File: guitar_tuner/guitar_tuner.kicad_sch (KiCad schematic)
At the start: 0 parts

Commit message: ESP32
ESP32 Addition
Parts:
- added C3, C4, C6: .1uF, symbol Device:C
- added C5: 1uF, symbol Device:C
- added R1: 10k, symbol Device:R
- added SW1: Reset, symbol Switch:SW_Omron_B3FS
- added SW2: Boot, symbol Switch:SW_Omron_B3FS
- added U1: ESP32-S2-SOLO, PCM_Espressif:ESP32-S2-SOLO, symbol esp32:ESP32-S2-SOLO
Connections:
- new net: C4.1, SW2.1, U1.39 (GPIO1/TOUCH1/ADC1_CH0)
- new net +3.3V: C3.2, C5.2, C6.2, R1.1, R1.2, SW1.2, U1.2 (3V3), U1.3 (EN)
- new net GND: C3.1, C4.2, C5.1, C6.1, SW1.1, SW2.2, U1.1 (GND), U1.40 (GND), U1.41 (GND)
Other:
- note added: "ESP32S2"

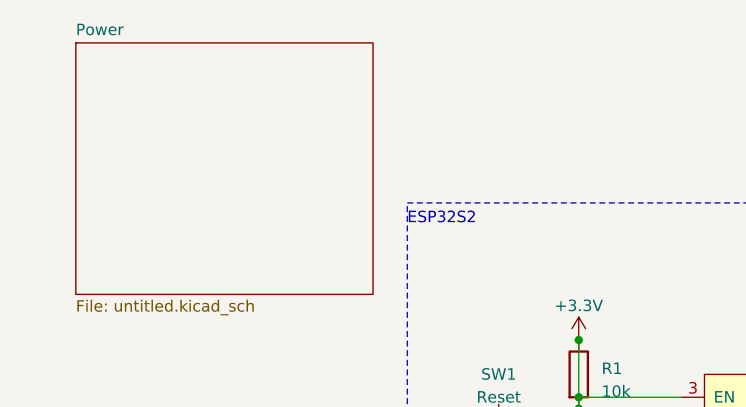
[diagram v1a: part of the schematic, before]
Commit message: Added micro USB B for input power as well as voltage regulator.
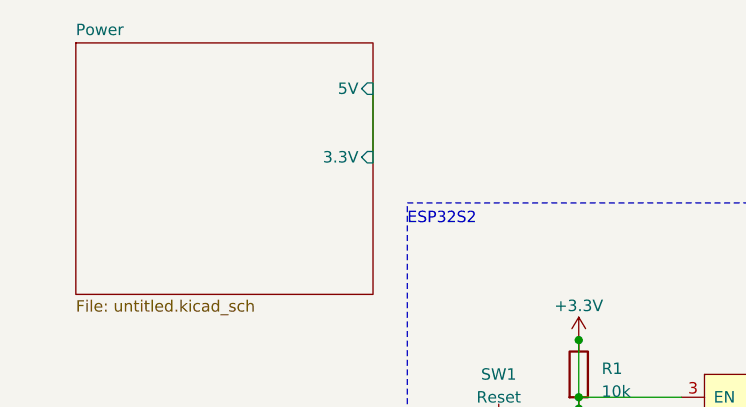
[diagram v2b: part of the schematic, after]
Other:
- sheet Power ports: added 3.3V, 5V; removed none
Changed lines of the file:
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@@
+	(wire
+		(pts
+			(xy 57.15 27.94) (xy 57.15 35.56)
+		)
+		(stroke
+			(width 0)
+			(type default)
+		)
+	)
 	(wire
 		(pts
@@
 			)
 		)
+		(pin "5V" input
+			(at 57.15 27.94 0)
+			(effects
+				(font
+					(size 1.27 1.27)
+				)
+				(justify right)
+			)
+		)
+		(pin "3.3V" input
+			(at 57.15 35.56 0)
+			(effects
+				(font
+					(size 1.27 1.27)
+				)
+				(justify right)
+			)
+		)

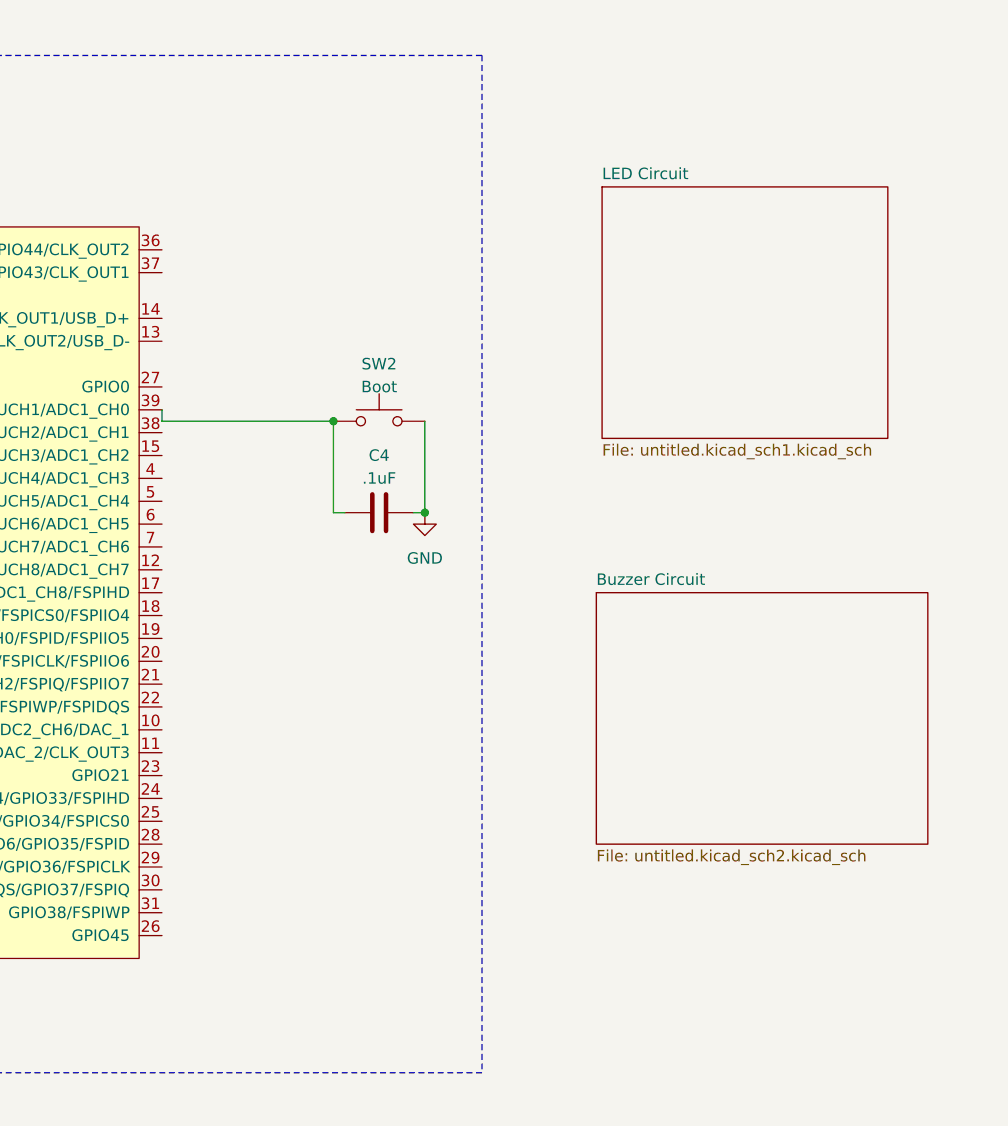
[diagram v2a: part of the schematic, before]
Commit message: LED
Addition of LED Circuits
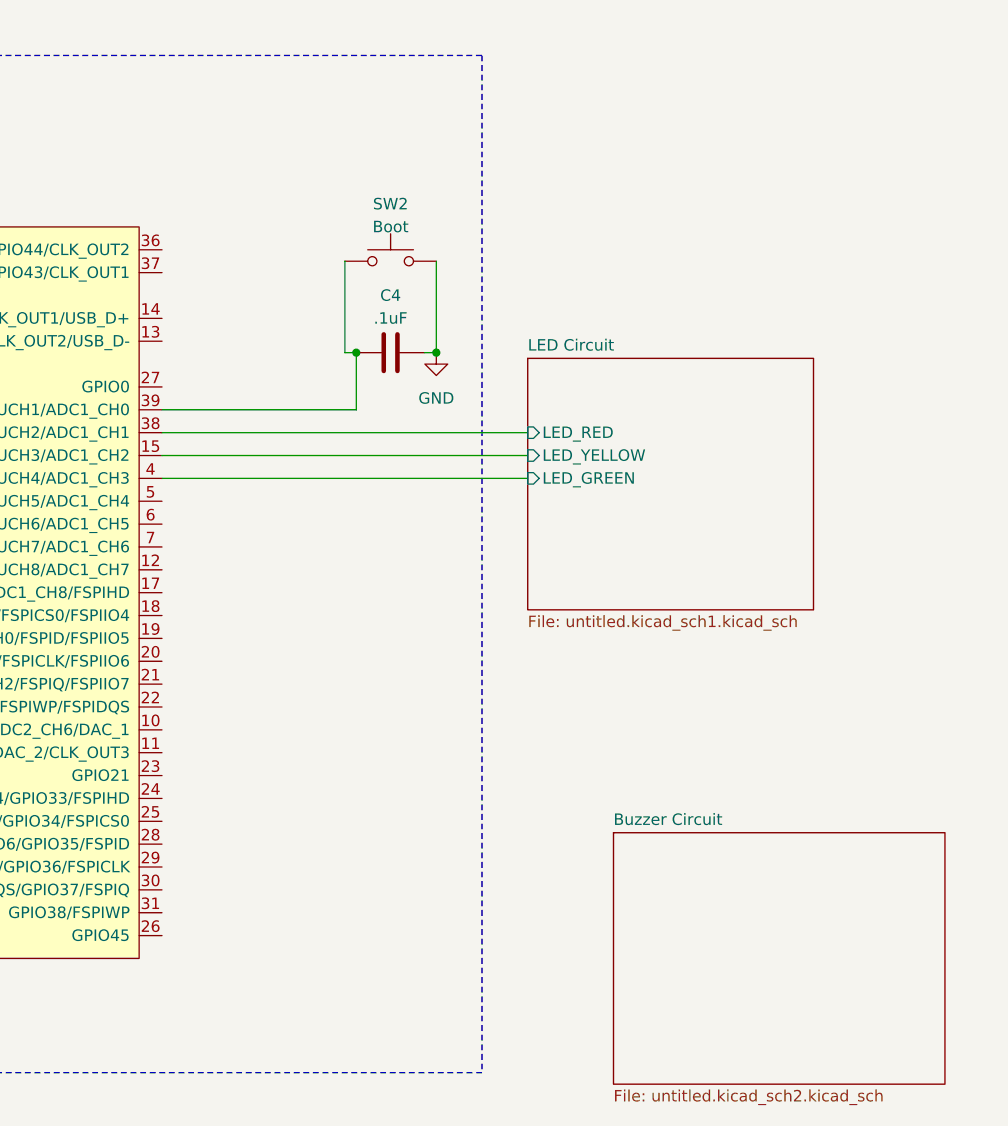
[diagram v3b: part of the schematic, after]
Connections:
- net LED Circuit/LED_YELLOW: now reaches U1.15 (GPIO3/TOUCH3/ADC1_CH2)
- net LED Circuit/LED_RED: now reaches U1.38 (GPIO2/TOUCH2/ADC1_CH1)
- net LED Circuit/LED_GREEN: now reaches U1.4 (GPIO4/TOUCH4/ADC1_CH3)
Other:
- sheet LED Circuit ports: added LED_GREEN, LED_RED, LED_YELLOW; removed none
- moved on the sheet: C4, SW2
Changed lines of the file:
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@@
 	)
 	(junction
-		(at 212.09 91.44)
-		(diameter 0)
-		(color 0 0 0 0)
-	)
-	(junction
-		(at 201.93 81.28)
+		(at 213.36 73.66)
 		(diameter 0)
 		(color 0 0 0 0)
@@
 		(color 0 0 0 0)
 	)
+	(junction
+		(at 204.47 73.66)
+		(diameter 0)
+		(color 0 0 0 0)
+	)
 	(wire
 		(pts
@@
 	(wire
 		(pts
-			(xy 203.2 91.44) (xy 201.93 91.44)
-		)
-		(stroke
-			(width 0)
-			(type default)
-		)
-	)
-	(wire
-		(pts
-			(xy 212.09 91.44) (xy 210.82 91.44)
+			(xy 204.47 73.66) (xy 203.2 73.66)
+		)
+		(stroke
+			(width 0)
+			(type default)
+		)
+	)
+	(wire
+		(pts
+			(xy 182.88 87.63) (xy 223.52 87.63)
+		)
+		(stroke
+			(width 0)
+			(type default)
+		)
+	)
+	(wire
+		(pts
+			(xy 213.36 73.66) (xy 212.09 73.66)
 		)
 		(stroke
@@
 	(wire
 		(pts
+			(xy 204.47 73.66) (xy 204.47 80.01)
+		)
+		(stroke
+			(width 0)
+			(type default)
+		)
+	)
+	(wire
+		(pts
+			(xy 182.88 80.01) (xy 204.47 80.01)
+		)
+		(stroke
+			(width 0)
+			(type default)
+		)
+	)
+	(wire
+		(pts
 			(xy 80.01 62.23) (xy 91.44 62.23)
 		)
@@
 	(wire
 		(pts
-			(xy 212.09 81.28) (xy 212.09 91.44)
-		)
-		(stroke
-			(width 0)
-			(type default)
-		)
-	)
-	(wire
-		(pts
-			(xy 182.88 81.28) (xy 201.93 81.28)
+			(xy 213.36 63.5) (xy 213.36 73.66)
 		)
 		(stroke
@@
 	(wire
 		(pts
-			(xy 201.93 81.28) (xy 201.93 91.44)
+			(xy 203.2 63.5) (xy 203.2 73.66)
+		)
+		(stroke
+			(width 0)
+			(type default)
+		)
+	)
+	(wire
+		(pts
+			(xy 182.88 82.55) (xy 223.52 82.55)
+		)
+		(stroke
+			(width 0)
+			(type default)
+		)
+	)
+	(wire
+		(pts
+			(xy 182.88 85.09) (xy 223.52 85.09)
 		)
 		(stroke
@@
 		(pts
 			(xy 80.01 66.04) (xy 76.2 66.04)
-		)
-		(stroke
-			(width 0)
-			(type default)
-		)
-	)
-	(wire
-		(pts
-			(xy 182.88 80.01) (xy 182.88 81.28)
 		)
 		(stroke
@@
 	(symbol
 		(lib_id "Switch:SW_Omron_B3FS")
-		(at 207.01 81.28 0)
+		(at 208.28 63.5 0)
 		(unit 1)
 		(exclude_from_sim no)
@@
 		(fields_autoplaced yes)
 		(property "Reference" "SW2"
-			(at 207.01 74.93 0)
+			(at 208.28 57.15 0)
 			(effects
 				(font
@@
 		)
 		(property "Value" "Boot"
-			(at 207.01 77.47 0)
+			(at 208.28 59.69 0)
 			(effects
 				(font
@@
 		)
 		(property "Footprint" ""
-			(at 207.01 76.2 0)
+			(at 208.28 58.42 0)
 			(effects
 				(font
@@
 		)
 		(property "Datasheet" "https://omronfs.omron.com/en_US/ecb/products/pdf/en-b3fs.pdf"
-			(at 207.01 76.2 0)
+			(at 208.28 58.42 0)
 			(effects
 				(font
@@
 		)
 		(property "Description" ""
-			(at 207.01 81.28 0)
+			(at 208.28 63.5 0)
 			(effects
 				(font
@@
 	(symbol
 		(lib_id "Device:C")
-		(at 207.01 91.44 90)
+		(at 208.28 73.66 90)
 		(unit 1)
 		(exclude_from_sim no)
@@
 		(fields_autoplaced yes)
 		(property "Reference" "C4"
-			(at 207.01 85.09 90)
+			(at 208.28 67.31 90)
 			(effects
 				(font
@@
 		)
 		(property "Value" ".1uF"
-			(at 207.01 87.63 90)
+			(at 208.28 69.85 90)
 			(effects
 				(font
@@
 		)
 		(property "Footprint" ""
-			(at 210.82 90.4748 0)
+			(at 212.09 72.6948 0)
 			(effects
 				(font
@@
 		)
 		(property "Datasheet" "~"
-			(at 207.01 91.44 0)
+			(at 208.28 73.66 0)
 			(effects
 				(font
@@
 		)
 		(property "Description" ""
-			(at 207.01 91.44 0)
+			(at 208.28 73.66 0)
 			(effects
 				(font
@@
 	(symbol
 		(lib_id "power:GND")
-		(at 212.09 91.44 0)
+		(at 213.36 73.66 0)
 		(unit 1)
 		(exclude_from_sim no)
@@
 		(fields_autoplaced yes)
 		(property "Reference" "#PWR07"
-			(at 212.09 97.79 0)
+			(at 213.36 80.01 0)
 			(effects
 				(font
@@
 		)
 		(property "Value" "GND"
-			(at 212.09 96.52 0)
+			(at 213.36 78.74 0)
 			(effects
 				(font
@@
 		)
 		(property "Footprint" ""
-			(at 212.09 91.44 0)
+			(at 213.36 73.66 0)
 			(effects
 				(font
@@
 		)
 		(property "Datasheet" ""
-			(at 212.09 91.44 0)
+			(at 213.36 73.66 0)
 			(effects
 				(font
@@
 		)
 		(property "Description" ""
-			(at 212.09 91.44 0)
+			(at 213.36 73.66 0)
 			(effects
 				(font
@@
 	)
 	(sheet
-		(at 231.775 55.245)
+		(at 223.52 74.295)
 		(size 31.75 27.94)
 		(exclude_from_sim no)
@@
 		)
 		(property "Sheetname" "LED Circuit"
-			(at 231.775 54.5334 0)
+			(at 223.52 73.5834 0)
 			(effects
 				(font
@@
 		)
 		(property "Sheetfile" "untitled.kicad_sch1.kicad_sch"
-			(at 231.775 83.7696 0)
+			(at 223.52 102.8196 0)
 			(effects
 				(font
@@
 				)
 				(justify left top)
+			)
+		)
+		(pin "LED_RED" input
+			(at 223.52 82.55 180)
+			(effects
+				(font
+					(size 1.27 1.27)
+				)
+				(justify left)
+			)
+		)
+		(pin "LED_GREEN" input
+			(at 223.52 87.63 180)
+			(effects
+				(font
+					(size 1.27 1.27)
+				)
+				(justify left)
+			)
+		)
+		(pin "LED_YELLOW" input
+			(at 223.52 85.09 180)
+			(effects
+				(font
+					(size 1.27 1.27)
+				)
+				(justify left)
 			)
 		)
@@
 	)
 	(sheet
-		(at 231.14 100.33)
+		(at 233.045 127)
 		(size 36.83 27.94)
 		(exclude_from_sim no)
@@
 		)
 		(property "Sheetname" "Buzzer Circuit"
-			(at 231.14 99.6184 0)
+			(at 233.045 126.2884 0)
 			(effects
 				(font
@@
 		)
 		(property "Sheetfile" "untitled.kicad_sch2.kicad_sch"
-			(at 231.14 128.8546 0)
-			(effects
-				(font
+			(at 233.045 155.5246 0)
+			(effects
+				(font

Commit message: OLED
Addition of OLED Screen
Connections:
- net SCL: now reaches U1.6 (GPIO6/TOUCH6/ADC1_CH5)
- net SDA: now reaches U1.7 (GPIO7/TOUCH7/ADC1_CH6)
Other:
- sheet Display ports: added OLED, RESET, SCL, SDA; removed none
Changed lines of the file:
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@@
+	)
+	(junction
+		(at 66.04 66.04)
+		(diameter 0)
+		(color 0 0 0 0)
 	)
 	(junction
@@
 	(wire
 		(pts
+			(xy 57.15 87.63) (xy 57.15 66.04)
+		)
+		(stroke
+			(width 0)
+			(type default)
+		)
+	)
+	(wire
+		(pts
+			(xy 53.34 87.63) (xy 57.15 87.63)
+		)
+		(stroke
+			(width 0)
+			(type default)
+		)
+	)
+	(wire
+		(pts
 			(xy 76.2 66.04) (xy 76.2 74.93)
 		)
@@
 	(wire
 		(pts
+			(xy 57.15 66.04) (xy 66.04 66.04)
+		)
+		(stroke
+			(width 0)
+			(type default)
+		)
+	)
+	(wire
+		(pts
 			(xy 162.56 43.18) (xy 162.56 48.26)
 		)
@@
 	(wire
 		(pts
+			(xy 58.42 46.99) (xy 57.15 46.99)
+		)
+		(stroke
+			(width 0)
+			(type default)
+		)
+	)
+	(wire
+		(pts
 			(xy 137.16 53.34) (xy 137.16 57.15)
 		)
@@
 	(wire
 		(pts
+			(xy 53.34 91.44) (xy 58.42 91.44)
+		)
+		(stroke
+			(width 0)
+			(type default)
+		)
+	)
+	(wire
+		(pts
 			(xy 213.36 63.5) (xy 213.36 73.66)
 		)
@@
 	(wire
 		(pts
-			(xy 57.15 27.94) (xy 57.15 35.56)
+			(xy 58.42 91.44) (xy 58.42 46.99)
 		)
 		(stroke
@@
 			(width 0)
 			(type default)
+		)
+	)
+	(global_label "SCL"
+		(shape output)
+		(at 53.34 95.25 0)
+		(fields_autoplaced yes)
+		(effects
+			(font
+				(size 1.27 1.27)
+			)
+			(justify left)
+		)
+		(property "Intersheetrefs" "${INTERSHEET_REFS}"
+			(at 59.8328 95.25 0)
+			(effects
+				(font
+					(size 1.27 1.27)
+				)
+				(justify left)
+				(hide yes)
+			)
+		)
+	)
+	(global_label "SCL"
+		(shape output)
+		(at 182.88 92.71 0)
+		(fields_autoplaced yes)
+		(effects
+			(font
+				(size 1.27 1.27)
+			)
+			(justify left)
+		)
+		(property "Intersheetrefs" "${INTERSHEET_REFS}"
+			(at 189.3728 92.71 0)
+			(effects
+				(font
+					(size 1.27 1.27)
+				)
+				(justify left)
+				(hide yes)
+			)
+		)
+	)
+	(global_label "SDA"
+		(shape output)
+		(at 182.88 95.25 0)
+		(fields_autoplaced yes)
+		(effects
+			(font
+				(size 1.27 1.27)
+			)
+			(justify left)
+		)
+		(property "Intersheetrefs" "${INTERSHEET_REFS}"
+			(at 189.4333 95.25 0)
+			(effects
+				(font
+					(size 1.27 1.27)
+				)
+				(justify left)
+				(hide yes)
+			)
+		)
+	)
+	(global_label "SDA"
+		(shape output)
+		(at 53.34 97.79 0)
+		(fields_autoplaced yes)
+		(effects
+			(font
+				(size 1.27 1.27)
+			)
+			(justify left)
+		)
+		(property "Intersheetrefs" "${INTERSHEET_REFS}"
+			(at 59.8933 97.79 0)
+			(effects
+				(font
+					(size 1.27 1.27)
+				)
+				(justify left)
+				(hide yes)
+			)
 		)
 	)
@@
 	)
 	(sheet
-		(at 17.78 113.03)
+		(at 17.78 73.66)
 		(size 35.56 27.94)
 		(exclude_from_sim no)
@@
 		)
 		(property "Sheetname" "Display"
-			(at 17.78 112.3184 0)
+			(at 17.78 72.9484 0)
 			(effects
 				(font
@@
 		)
 		(property "Sheetfile" "untitled.kicad_sch4.kicad_sch"
-			(at 17.78 141.5546 0)
+			(at 17.78 102.1846 0)
 			(effects
 				(font
@@
 				)
 				(justify left top)
+			)
+		)
+		(pin "OLED" input
+			(at 53.34 91.44 0)
+			(effects
+				(font
+					(size 1.27 1.27)
+				)
+				(justify right)
+			)
+		)
+		(pin "RESET" input
+			(at 53.34 87.63 0)
+			(effects
+				(font
+					(size 1.27 1.27)
+				)
+				(justify right)
+			)
+		)
+		(pin "SCL" input
+			(at 53.34 95.25 0)
+			(effects
+				(font
+					(size 1.27 1.27)
+				)
+				(justify right)
+			)
+		)
+		(pin "SDA" input
+			(at 53.34 97.79 0)
+			(effects
+				(font
+					(size 1.27 1.27)
+				)
+				(justify right)
 			)
 		)
@@
 	)
 	(sheet
-		(at 18.415 74.93)
+		(at 20.32 120.015)
 		(size 34.29 27.94)
 		(exclude_from_sim no)
@@
 		)
 		(property "Sheetname" "Audio Input Circuit"
-			(at 18.415 74.2184 0)
+			(at 20.32 119.3034 0)
 			(effects
 				(font
@@
 		)
 		(property "Sheetfile" "untitled.kicad_sch3.kicad_sch"
-			(at 18.415 103.4546 0)
+			(at 20.32 148.5396 0)
 			(effects
 				(font
@@
 			)
 		)
+		(pin "3.3V" input
+			(at 57.15 46.99 0)
+			(effects
+				(font
+					(size 1.27 1.27)
+				)
+				(justify right)
+			)
+		)
 		(pin "5V" input
-			(at 57.15 27.94 0)
-			(effects
-				(font
-					(size 1.27 1.27)
-				)
-				(justify right)
-			)
-		)
-		(pin "3.3V" input
-			(at 57.15 35.56 0)
-			(effects
-				(font
+			(at 57.15 31.75 0)
+			(effects
+				(font
